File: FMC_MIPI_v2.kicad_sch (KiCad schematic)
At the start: 0 parts

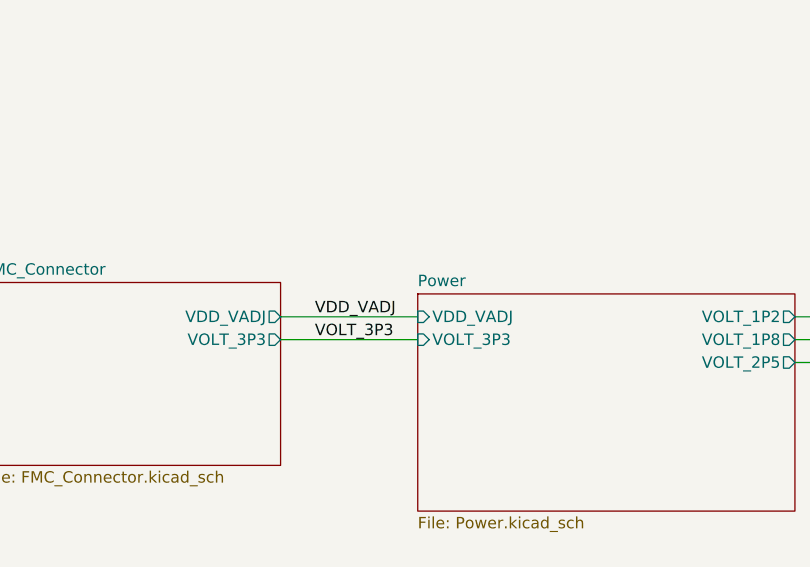
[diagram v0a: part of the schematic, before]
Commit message: DRC, ERC OK
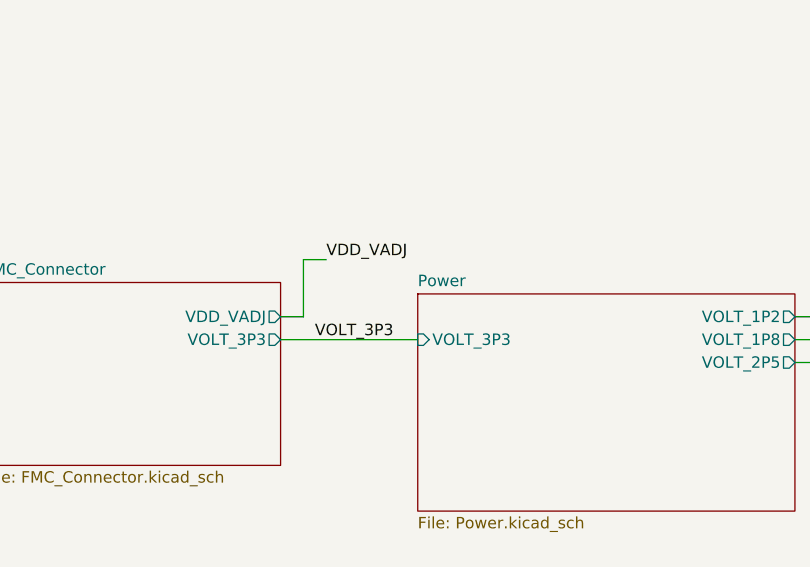
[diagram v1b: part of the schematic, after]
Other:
- sheet Power ports: added none; removed VDD_VADJ
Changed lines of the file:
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@@
     (stroke (width 0) (type default) (color 0 0 0 0))
   )
-  (wire (pts (xy 50.8 26.67) (xy 66.04 26.67))
+  (wire (pts (xy 50.8 26.67) (xy 53.34 26.67))
     (stroke (width 0) (type default) (color 0 0 0 0))
   )
@@
     (stroke (width 0) (type default) (color 0 0 0 0))
   )
+  (wire (pts (xy 53.34 26.67) (xy 53.34 20.32))
+    (stroke (width 0) (type default) (color 0 0 0 0))
+  )
   (polyline (pts (xy 21.59 139.7) (xy 50.8 139.7))
     (stroke (width 0) (type default) (color 0 0 0 0))
@@
   )
   (wire (pts (xy 107.95 31.75) (xy 115.57 31.75))
+    (stroke (width 0) (type default) (color 0 0 0 0))
+  )
+  (wire (pts (xy 53.34 20.32) (xy 55.88 20.32))
     (stroke (width 0) (type default) (color 0 0 0 0))
   )
@@
     (effects (font (size 1.27 1.27)) (justify left bottom))
   )
-  (label "VDD_VADJ" (at 54.61 26.67 0)
+  (label "VDD_VADJ" (at 55.88 20.32 0)
     (effects (font (size 1.27 1.27)) (justify left bottom))
   )
@@
     (pin "VOLT_1P8" output (at 107.95 29.21 0)
       (effects (font (size 1.27 1.27)) (justify right))
-    )
-    (pin "VDD_VADJ" input (at 66.04 26.67 180)
-      (effects (font (size 1.27 1.27)) (justify left))
     )
     (pin "VOLT_3P3" input (at 66.04 29.21 180)
@@
       (reference "#PWR0170") (unit 1) (value "Earth") (footprint "")
     )
+    (path "/00000000-0000-0000-0000-00006191d89c/a6e028eb-5cad-4a89-9ee1-8b000b9d29f8"
+      (reference "#PWR0171") (unit 1) (value "Earth") (footprint "")
+    )
+    (path "/00000000-0000-0000-0000-00006191d89c/1baeb4d8-9d24-4168-8d32-ec567582b332"
+      (reference "#PWR0172") (unit 1) (value "Earth") (footprint "")
+    )
     (path "/00000000-0000-0000-0000-00006191d89c/00000000-0000-0000-0000-00006384a0b1"
       (reference "C1") (unit 1) (value "0.1uF") (footprint "Capacitors_SMD:C_0402")
@@
     )
     (path "/00000000-0000-0000-0000-000061aca102/00000000-0000-0000-0000-0000635d4ce0"
-      (reference "D1") (unit 1) (value "UCLAMP0501H.TCT") (footprint "Diodes_SMD:D_SOD-523")
+      (reference "D1") (unit 1) (value "UCLAMP0501H.TCT") (footprint "SODFL1608X70N")
     )
     (path "/00000000-0000-0000-0000-0000637747ef/00000000-0000-0000-0000-0000636d55eb"
-      (reference "D2") (unit 1) (value "UCLAMP0501H.TCT") (footprint "Diodes_SMD:D_SOD-523")
+      (reference "D2") (unit 1) (value "UCLAMP0501H.TCT") (footprint "SODFL1608X70N")
     )
     (path "/00000000-0000-0000-0000-0000637747ef/00000000-0000-0000-0000-0000636d7d69"
-      (reference "D3") (unit 1) (value "UCLAMP0501H.TCT") (footprint "Diodes_SMD:D_SOD-523")
+      (reference "D3") (unit 1) (value "UCLAMP0501H.TCT") (footprint "SODFL1608X70N")
     )
     (path "/00000000-0000-0000-0000-0000637747ef/00000000-0000-0000-0000-0000636c2a4e"
-      (reference "D4") (unit 1) (value "UCLAMP0501H.TCT") (footprint "Diodes_SMD:D_SOD-523")
+      (reference "D4") (unit 1) (value "UCLAMP0501H.TCT") (footprint "SODFL1608X70N")
     )
     (path "/00000000-0000-0000-0000-00006191d89c/00000000-0000-0000-0000-000063727c9f"
@@
     )
     (path "/00000000-0000-0000-0000-00006362ecc5/00000000-0000-0000-0000-00006365cfd1"
-      (reference "IC3") (unit 1) (value "TCA9406DCUR") (footprint "FMC_MIPI_v2_sym:SOP50P310X90-8N")
+      (reference "IC3") (unit 1) (value "TCA9406DCUR") (footprint "SOP50P310X90-8N")
     )
     (path "/00000000-0000-0000-0000-00006362ecc5/00000000-0000-0000-0000-0000636b86ee"
-      (reference "IC4") (unit 1) (value "TCA9406DCUR") (footprint "FMC_MIPI_v2_sym:SOP50P310X90-8N")
+      (reference "IC4") (unit 1) (value "TCA9406DCUR") (footprint "SOP50P310X90-8N")
     )
     (path "/00000000-0000-0000-0000-00006362ecc5/00000000-0000-0000-0000-000063721435"
-      (reference "IC5") (unit 1) (value "TCA9406DCUR") (footprint "FMC_MIPI_v2_sym:SOP50P310X90-8N")
+      (reference "IC5") (unit 1) (value "TCA9406DCUR") (footprint "SOP50P310X90-8N")
     )
     (path "/00000000-0000-0000-0000-000061aca102/00000000-0000-0000-0000-000063729e09"
-      (reference "IC6") (unit 1) (value "SN74AVC1T45DCKT") (footprint "FMC_MIPI_v2_sym:SOT65P210X110-6N")
+      (reference "IC6") (unit 1) (value "SN74AVC1T45DCKT") (footprint "SOT65P210X110-6N")
     )
     (path "/00000000-0000-0000-0000-00006362ecc5/00000000-0000-0000-0000-000063b30661"
-      (reference "IC7") (unit 1) (value "SN74AVC1T45DCKT") (footprint "FMC_MIPI_v2_sym:SOT65P210X110-6N")
+      (reference "IC7") (unit 1) (value "SN74AVC1T45DCKT") (footprint "SOT65P210X110-6N")
     )
     (path "/00000000-0000-0000-0000-00006170b975/00000000-0000-0000-0000-00006191882c"
@@
     )
     (path "/00000000-0000-0000-0000-0000637747ef/00000000-0000-0000-0000-000063810b84"
-      (reference "U1") (unit 1) (value "LP5907MFX-1.8") (footprint "TO_SOT_Packages_SMD:SOT-23-5")
+      (reference "U1") (unit 1) (value "LP5907MFX-1.8") (footprint "Package_TO_SOT_SMD:SOT-23-5")
     )
     (path "/00000000-0000-0000-0000-000061aca102/00000000-0000-0000-0000-000063958435"
-      (reference "U2") (unit 1) (value "SN74AVC2T45DCUR") (footprint "FMC_MIPI_v2_sym:SN74AVC2T45DCUR")
+      (reference "U2") (unit 1) (value "SN74AVC2T45DCUR") (footprint "DCU8")
     )
     (path "/00000000-0000-0000-0000-00006362ecc5/00000000-0000-0000-0000-000063673675"
@@
     )
     (path "/00000000-0000-0000-0000-0000637747ef/00000000-0000-0000-0000-000063821542"
-      (reference "U7") (unit 1) (value "LP5907MFX-1.2") (footprint "TO_SOT_Packages_SMD:SOT-23-5")
+      (reference "U7") (unit 1) (value "LP5907MFX-1.2") (footprint "Package_TO_SOT_SMD:SOT-23-5")
     )
     (path "/00000000-0000-0000-0000-00006191d89c/00000000-0000-0000-0000-0000636800c7"

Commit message: JLCPCB BOM OK
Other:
- note added: "Stackup: Single Ended: 6 mil Differential: 4 mil Width, 8 mil spacing ----- 0.1 mm height to ground plane JLCPCB Stackup name: JLC06161H-3313"
- note removed: "Stackup: Single Ended: 6 mil Differential: 4 mil Width, 8 mil spacing ----- 0.1 mm height to ground plane"
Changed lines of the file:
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@@
     (effects (font (size 1.27 1.27)) (justify left bottom))
   )
-  (text "Stackup:\nSingle Ended: 6 mil\nDifferential:\n4  mil Width, 8 mil spacing\n-----\n0.1 mm height to ground plane\n"
-    (at 58.42 154.94 0)
-    (effects (font (size 1.27 1.27)) (justify left bottom))
+  (text "Stackup:\nSingle Ended: 6 mil\nDifferential:\n4  mil Width, 8 mil spacing\n-----\n0.1 mm height to ground plane\n\nJLCPCB Stackup name: JLC06161H-3313\n"
+    (at 55.88 163.195 0)
+    (effects (font (size 2 2) (thickness 0.254) bold) (justify left bottom))
   )
   (label "VOLT_3P3" (at 54.61 29.21 0)
@@
     )
     (path "/00000000-0000-0000-0000-000061aca102/00000000-0000-0000-0000-0000637a2fc5"
-      (reference "R29") (unit 1) (value "1k") (footprint "Resistors_SMD:R_0805")
+      (reference "R29") (unit 1) (value "2.2k") (footprint "Resistors_SMD:R_0805")
     )
     (path "/00000000-0000-0000-0000-000061aca102/00000000-0000-0000-0000-00006376ce9d"
@@
     )
     (path "/00000000-0000-0000-0000-00006362ecc5/00000000-0000-0000-0000-0000638632db"
-      (reference "R31") (unit 1) (value "1k") (footprint "Resistors_SMD:R_0805")
+      (reference "R31") (unit 1) (value "2.2k") (footprint "Resistors_SMD:R_0805")
     )
     (path "/00000000-0000-0000-0000-000061aca102/00000000-0000-0000-0000-0000638d5ec5"
-      (reference "R32") (unit 1) (value "1k") (footprint "Resistors_SMD:R_0805")
+      (reference "R32") (unit 1) (value "2.2k") (footprint "Resistors_SMD:R_0805")
     )
     (path "/00000000-0000-0000-0000-000061aca102/00000000-0000-0000-0000-0000638d5eb1"
@@
     )
     (path "/00000000-0000-0000-0000-000061aca102/00000000-0000-0000-0000-000063a1f4ee"
-      (reference "R34") (unit 1) (value "1k") (footprint "Resistors_SMD:R_0805")
+      (reference "R34") (unit 1) (value "2.2k") (footprint "Resistors_SMD:R_0805")
     )
     (path "/00000000-0000-0000-0000-00006362ecc5/00000000-0000-0000-0000-000063b3066e"
@@
     )
     (path "/00000000-0000-0000-0000-00006362ecc5/00000000-0000-0000-0000-000063673675"
-      (reference "U3") (unit 1) (value "SN74AVCH16T245_DGV_48") (footprint "FMC_MIPI_v2_sym:DGV48")
+      (reference "U3") (unit 1) (value "SN74AVCH16T245GR") (footprint "FMC_MIPI_v2_sym:SOP50P810X120-48N")
     )
     (path "/00000000-0000-0000-0000-0000637747ef/00000000-0000-0000-0000-00006379d961"
@@
     )
     (path "/00000000-0000-0000-0000-00006191d89c/00000000-0000-0000-0000-0000636800c7"
-      (reference "U8") (unit 1) (value "SN74AVCH16T245_DGV_48") (footprint "FMC_MIPI_v2_sym:DGV48")
-    )
-  )
+      (reference "U8") (unit 1) (value "SN74AVCH16T245GR") (footprint "FMC_MIPI_v2_sym:SOP50P810X120-48N")
+    )
+  )
